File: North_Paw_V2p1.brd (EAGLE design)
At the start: 53.5 x 38.5 mm, 19 parts, among them Q1 8MHz

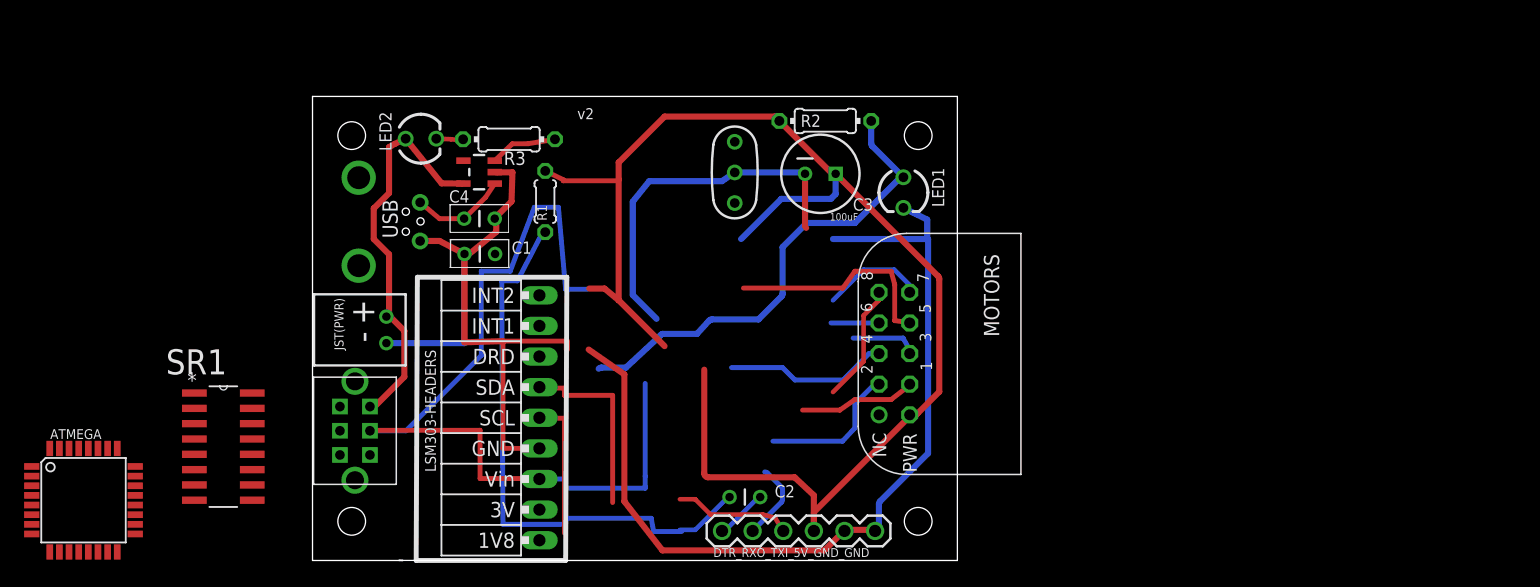
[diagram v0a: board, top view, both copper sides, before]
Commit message: More smd and routing updates
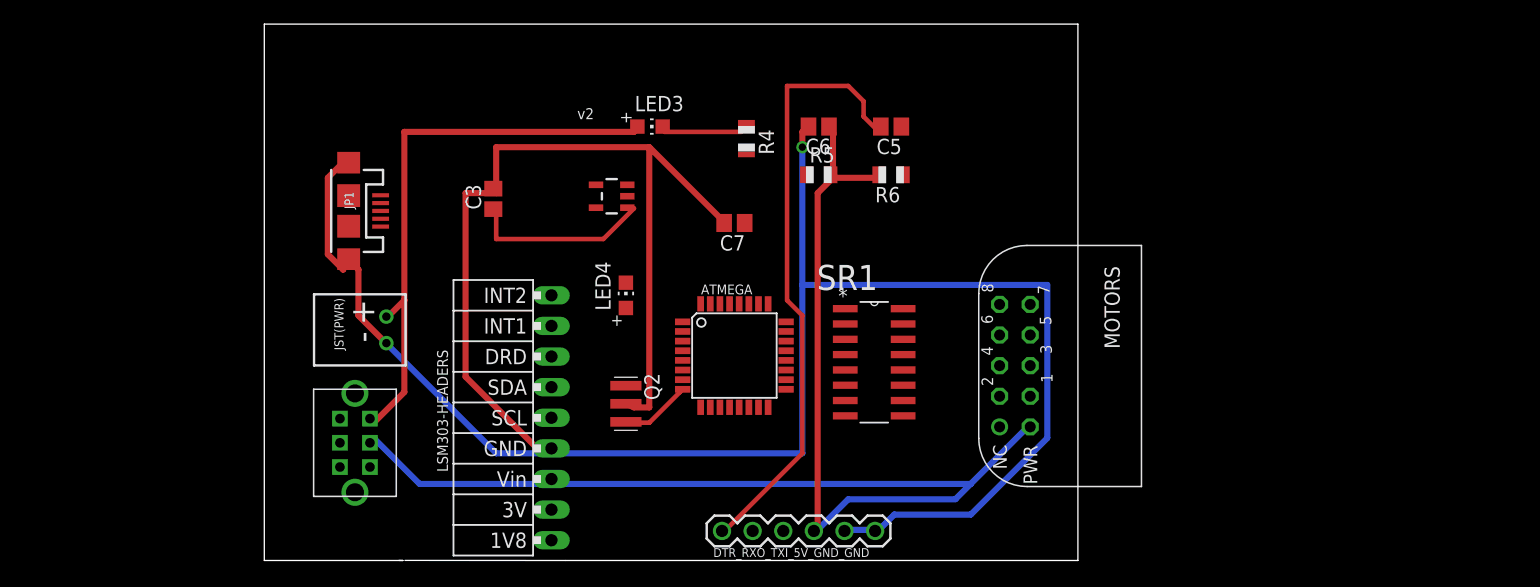
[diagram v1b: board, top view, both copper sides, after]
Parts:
- removed C1, C2: 0.1uF, SparkFun:CAP-PTH-SMALL
- removed C4: 1uF, SparkFun:CAP-PTH-SMALL
- removed LED1: GREEN, SparkFun:LED3MM
- removed LED2: RED, SparkFun:LED3MM
- removed Q1: 8MHz, SparkFun:RESONATOR-PTH
- removed R1: 10k, resistor:0204/5
- removed R2: 10k, resistor:0204/7
- removed R3: 330, resistor:0204/7
- removed USB: USB-MB-H, North_Paw:USB-MB-H
- added C5, C7: 0.1uF, adafruit:C0805
- added C6: 100uf, adafruit:C0805
- added JP1: USB-MICROB, SparkFun-Connectors:USB-MICROB
- added LED3: RED, adafruit:CHIP-LED0805
- added LED4: GREEN, adafruit:CHIP-LED0805
- added Q2: 8MHz, murata-filter:CSTCR6M
- added R4: 330, adafruit:R0805
- added R5, R6: 10k, adafruit:R0805
- C3: value 100uF -> 1uF; device SparkFun:CPOL-RADIAL-100UF-25V -> adafruit:C0805
- moved ATMEGA 55.3 mm to (35.0, 17.0)
- moved SR1 54.5 mm to (49.0, 12.0)
- moved C3 27.2 mm to (15.0, 30.0), turned to 90 degrees
- moved CHARGER 11.2 mm to (24.8, 30.2)
- moved MOTORS 10.0 mm to (63.3, 16.1)
- moved LSM303-HEADERS 1.00 mm to (19.8, 11.8)
- moved SWITCH 1.00 mm to (3.52, 9.76)
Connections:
- removed net N$9: LED2.K, R3.1
- new net N$8: LED3.C, R4.1
- net 3.3V: now also C6.1, R5.2, R6.2; no longer C3.1, R1.2, R2.2
- net A0: now also LED4.A, R5.1; no longer LED1.A, R2.1
- net BATT: now also LED3.A; no longer LED2.A
- net DTR: now also C5.2; no longer C2.2
- net GND: now also C6.2, C7.2, JP1.GND, JP1.MT1, JP1.MT2, LED4.C, Q2.2; no longer C1.1, C4.2, LED1.K, Q1.2, USB.GND
- net N$1: now also Q2.1; no longer Q1.3
- net N$2: now also Q2.3; no longer Q1.1
- net N$3: now also C7.1; no longer C1.2
- net N$7: now also R4.2; no longer R3.2
- net RESET: now also C5.1, R6.1; no longer C2.1, R1.1
- net USB_VIN: now also C3.1, JP1.VBUS; no longer C4.1, USB.VBUS
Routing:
- net GND: track 128.5 -> 216.9 mm, vias 0 -> 1
- net 3.3V: track 161.0 -> 112.8 mm
- net RESET: track 47.7 -> 0.00 mm
- net DTR: track 4.28 -> 50.7 mm
- net A0: track 39.9 -> 0.00 mm
- net N$6: track 35.0 -> 0.08 mm
- net M6: track 18.7 -> 0.00 mm
- net N$5: track 18.2 -> 0.00 mm
- net A4: track 15.6 -> 0.00 mm
- net BATT: track 32.9 -> 47.3 mm
- net M3: track 13.6 -> 0.00 mm
- net N$4: track 13.0 -> 0.00 mm
- net M1: track 12.0 -> 0.00 mm
- net A5: track 11.6 -> 0.00 mm
- net M7: track 9.85 -> 0.00 mm
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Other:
- board size 53.5 x 38.5 mm -> 67.5 x 44.5 mm
- board text removed: "<-Off On->"
- board text removed: "RES 8Mhz"

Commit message: Initial checkin of TopoR
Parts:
- removed SWITCH: OS202011MA0QS1, OS202011MA0QS1:OS202011MA0QS1
- added S1: (no value), SparkFun-Electromechanical:SWITCH-SPST-SMD-A
- moved JP1 60.2 mm to (61.0, 13.0), turned to 0 degrees
- moved FTDI 48.4 mm to (72.0, 32.5)
- moved JST(PWR) 47.4 mm to (52.0, 31.0), turned to 180 degrees
- moved LED4 44.4 mm to (70.0, 16.0), turned to 90 degrees
- moved C3 40.5 mm to (54.0, 19.0), turned to 180 degrees
- moved C6 39.6 mm to (81.0, 29.0), turned to 0 degrees
- moved R6 39.0 mm to (84.0, 17.0), turned to 270 degrees
- moved SR1 37.7 mm to (84.0, 26.0), turned to 90 degrees
- moved R5 35.8 mm to (74.0, 16.0)
- moved Q2 33.5 mm to (58.0, 23.0)
- moved C7 33.1 mm to (68.0, 31.0)
- moved CHARGER 32.4 mm to (52.8, 13.8), turned to 180 degrees
- moved MOTORS 31.8 mm to (94.3, 23.1)
- moved ATMEGA 31.6 mm to (66.0, 23.0)
- moved LED3 27.7 mm to (53.0, 24.0), turned to 0 degrees
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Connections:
- removed net 1: SWITCH.1
- removed net 2: SWITCH.2
- removed net 3: SWITCH.3
- removed net 4: SWITCH.4
- new net N$4: JST(PWR).PWR, S1.3
- net 3.3V: now also S1.2; no longer SWITCH.5
- net BATT: no longer JST(PWR).PWR, SWITCH.6
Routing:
- net GND: track 216.9 -> 132.6 mm, vias 1 -> 2
- net 3.3V: track 112.8 -> 169.7 mm
- net DTR: track 50.7 -> 3.02 mm
- net D2: track 0.00 -> 34.3 mm, vias 0 -> 2
- net BATT: track 47.3 -> 18.3 mm
- net M2: track 0.00 -> 26.7 mm
- net M4: track 0.00 -> 26.3 mm
- net RESET: track 0.00 -> 19.0 mm, vias 0 -> 2
- net M5: track 0.00 -> 13.0 mm
- net M3: track 0.00 -> 12.1 mm, vias 0 -> 1
- net N$4: track 0.00 -> 11.2 mm, vias 0 -> 1
- net USB_VIN: track 15.8 -> 4.86 mm
- net N$2: track 5.86 -> 0.00 mm
- net N$8: track 7.44 -> 4.05 mm
- net A0: track 0.00 -> 2.00 mm
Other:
- board outline removed
- board text removed: "X:/Dropbox/Sensebridge/eagle/bmps/North_Paw_JUST_NP.bmp"
- board text removed: "v2"
